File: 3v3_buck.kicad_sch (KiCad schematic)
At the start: 7 parts, among them U1101 TLV62569DBVR

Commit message: added net tie to stepper motor PGND + various routing
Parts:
- NT1101: footprint BR_Virtual_Parts:NetTie-2_SMD_Pad_3.88mm_wide -> BR_Virtual_Parts:NetTie-2_SMD_Pad_0.18mm_wide; symbol BR_Virtual_Parts:NetTie-2_3.88mm -> BR_Virtual_Parts:NetTie-2_0.18mm
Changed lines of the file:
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@@
 	)
 	(symbol
-		(lib_id "BR_Virtual_Parts:NetTie-2_3.88mm")
+		(lib_id "BR_Virtual_Parts:NetTie-2_0.18mm")
 		(at 130.81 106.68 90)
 		(unit 1)
-		(exclude_from_sim yes)
+		(exclude_from_sim no)
 		(in_bom no)
 		(on_board yes)
@@
 			)
 		)
-		(property "Footprint" "BR_Virtual_Parts:NetTie-2_SMD_Pad_3.88mm_wide"
-			(at 130.81 106.68 0)
+		(property "Footprint" "BR_Virtual_Parts:NetTie-2_SMD_Pad_0.18mm_wide"
+			(at 131.064 105.664 90)
 			(effects
 				(font
@@
 		)
 		(property "Datasheet" "~"
-			(at 130.81 106.68 0)
+			(at 125.73 97.79 0)
 			(effects
 				(font
@@
 		)
 		(property "Manufacturer" "~"
-			(at 130.81 106.68 0)
+			(at 111.76 104.14 0)
 			(effects
 				(font
 					(size 1.27 1.27)
 				)
+				(justify left)
 				(hide yes)
 			)
 		)
 		(property "Supplier 1" "~"
-			(at 130.81 106.68 0)
+			(at 109.22 104.14 0)
 			(effects
 				(font
 					(size 1.27 1.27)
 				)
+				(justify left)
 				(hide yes)
 			)
 		)
 		(property "Supplier Part Num 1" "~"
-			(at 130.81 106.68 0)
+			(at 106.68 104.14 0)
 			(effects
 				(font
 					(size 1.27 1.27)
 				)
+				(justify left)
 				(hide yes)
 			)
 		)
 		(property "Supplier 2" "~"
-			(at 130.81 106.68 0)
+			(at 104.14 104.14 0)
 			(effects
 				(font
 					(size 1.27 1.27)
 				)
+				(justify left)
 				(hide yes)
 			)
 		)
 		(property "Supplier Part Num 2" "~"
-			(at 130.81 106.68 0)
+			(at 101.6 104.14 0)
 			(effects
 				(font
 					(size 1.27 1.27)
 				)
+				(justify left)
 				(hide yes)
 			)
 		)
 		(property "Supplier 3" "~"
-			(at 130.81 106.68 0)
+			(at 99.06 104.14 0)
 			(effects
 				(font
 					(size 1.27 1.27)
 				)
+				(justify left)
 				(hide yes)
 			)
 		)
 		(property "Supplier Part Num 3" "~"
-			(at 130.81 106.68 0)
+			(at 96.52 104.14 0)
 			(effects
 				(font
 					(size 1.27 1.27)
 				)
+				(justify left)
 				(hide yes)
 			)
 		)
 		(property "Manufacturer Part Num" "~"
-			(at 130.81 106.68 0)
+			(at 93.98 104.14 0)
 			(effects
 				(font
 					(size 1.27 1.27)
 				)
+				(justify left)
 				(hide yes)
 			)

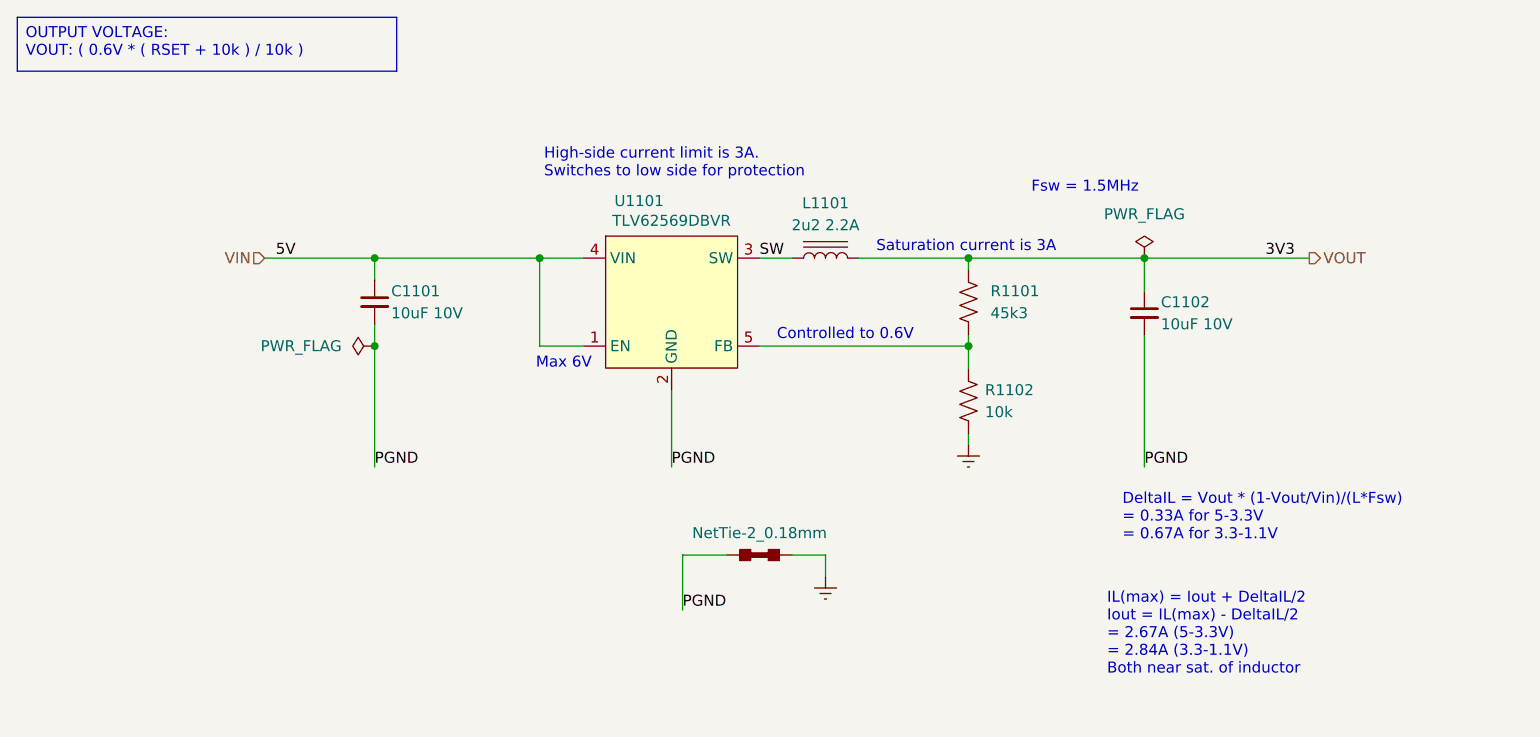
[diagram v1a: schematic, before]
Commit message: adding test pads + minor schematic edits
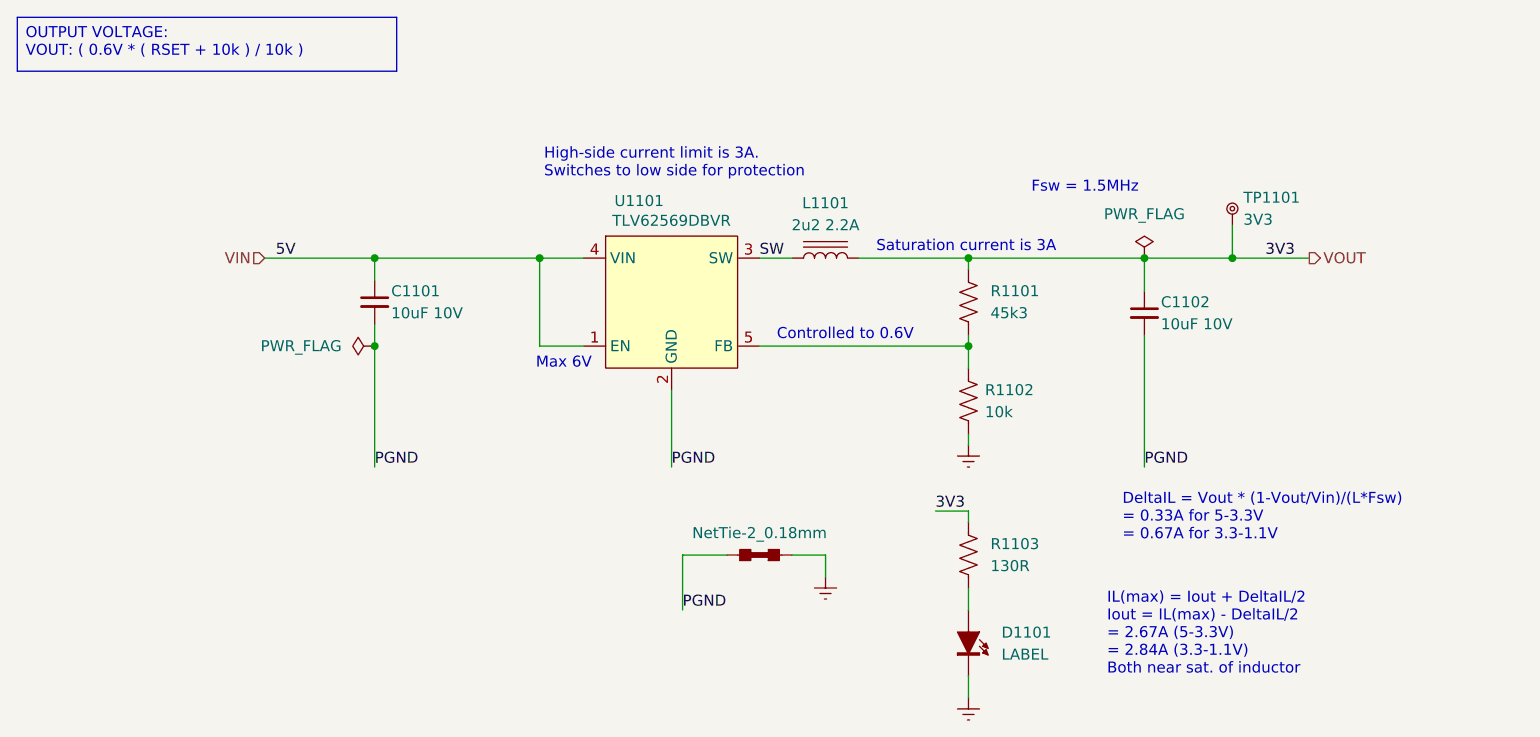
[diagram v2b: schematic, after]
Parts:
- added D1101: LABEL, BR_Optoelectronics:LED_0603_1608Metric, symbol BR_Optoelectronic:LTST-C191KGKT
- added R1103: 130R, BR_Passives:C_0402_1005Metric-minimized, symbol BR_Resistors_0402:R_0402_130R
- added TP1101: 3V3, BR_Connectors:TEST-TH_BD2.54-P1.4_RED, symbol BR_Connectors:TP_Ring_PTH
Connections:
- net GND: now also D1101.1 (K)
- net VOUT: now also R1103.1, TP1101.1
- new net: D1101.2 (A), R1103.2

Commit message: preboard review of updates
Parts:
- R1103: value 130R -> 1k3; symbol BR_Resistors_0402:R_0402_130R -> BR_Resistors_0402:R_0402_1k3; BRE Number BRE-000301 -> BRE-001251; JLCPCB Part Num C477610 -> C185455; Manufacturer Part Num RC0402FR-07130RL -> RC0402FR-071K3L; Supplier 2 Mouser -> DigiKey; Supplier Part Num 1 311-130LRCT-ND -> YAG3036CT-ND; Supplier Part Num 2 603-RC0402FR-07130RL -> YAG3036CT-ND; Supplier Part Num 3 C477610 -> C185455
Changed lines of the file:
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@@
 	)
 	(symbol
-		(lib_id "BR_Resistors_0402:R_0402_130R")
+		(lib_id "BR_Resistors_0402:R_0402_1k3")
 		(at 154.94 106.68 0)
 		(unit 1)
@@
 			)
 		)
-		(property "Value" "130R"
+		(property "Value" "1k3"
 			(at 157.48 107.9499 0)
 			(effects
@@
 			)
 		)
-		(property "Description" "130R 1% 100ppm 62.5mW Thick Film Resistor 0402"
+		(property "Description" "1.3k 1% 100ppm 62.5mW Thick Film Resistor 0402"
 			(at 154.94 43.18 0)
 			(effects
@@
 			)
 		)
-		(property "Manufacturer Part Num" "RC0402FR-07130RL"
+		(property "Manufacturer Part Num" "RC0402FR-071K3L"
 			(at 154.94 38.1 0)
 			(effects
@@
 			)
 		)
-		(property "BRE Number" "BRE-000301"
+		(property "BRE Number" "BRE-001251"
 			(at 154.94 40.64 0)
 			(effects
@@
 			)
 		)
-		(property "Supplier Part Num 1" "311-130LRCT-ND"
+		(property "Supplier Part Num 1" "YAG3036CT-ND"
 			(at 154.94 48.26 0)
 			(effects
@@
 			)
 		)
-		(property "Supplier 2" "Mouser"
+		(property "Supplier 2" "DigiKey"
 			(at 154.94 50.8 0)
 			(effects
@@
 			)
 		)
-		(property "Supplier Part Num 2" "603-RC0402FR-07130RL"
+		(property "Supplier Part Num 2" "YAG3036CT-ND"
 			(at 154.94 53.34 0)
 			(effects
@@
 			)
 		)
-		(property "Supplier Part Num 3" "C477610"
+		(property "Supplier Part Num 3" "C185455"
 			(at 154.94 58.42 0)
 			(effects
@@
 			)
 		)
-		(property "JLCPCB Part Num" "C477610"
+		(property "JLCPCB Part Num" "C185455"
 			(at 154.94 60.96 0)
 			(effects

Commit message: various improvements
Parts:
- D1101: value LABEL -> 3V3
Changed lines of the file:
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@@
 			)
 		)
-		(property "Value" "LABEL"
+		(property "Value" "3V3"
 			(at 158.75 118.1734 90)
 			(effects

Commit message: last checks + board characteristics tables
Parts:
- added TP1102: GND, BR_Connectors:TEST-TH_BD2.54-P1.4_RED, symbol BR_Connectors:TP_Ring_PTH
- C1101, C1102: JLCPCB Part Num (none) -> C315248
- L1101: JLCPCB Part Num (none) -> C2041550
- R1102: JLCPCB Part Num (none) -> C106225
- U1101: JLCPCB Part Num (none) -> C141836
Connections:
- net GND: now also TP1102.1

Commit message: refactoring tx a bit
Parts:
- NT1101: value NetTie-2_0.18mm -> Net_Tie_0201; footprint BR_Virtual_Parts:NetTie-2_SMD_Pad_0.18mm_wide -> BR_Virtual_Parts:Net_Tie_0201_1608Metric; symbol BR_Virtual_Parts:NetTie-2_0.18mm -> BR_Virtual_Parts:Net_Tie_0201
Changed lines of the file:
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@@
 	)
 	(symbol
-		(lib_id "BR_Virtual_Parts:NetTie-2_0.18mm")
+		(lib_id "BR_Virtual_Parts:Net_Tie_0201")
 		(at 130.81 106.68 90)
 		(unit 1)
@@
 			)
 		)
-		(property "Value" "NetTie-2_0.18mm"
+		(property "Value" "Net_Tie_0201"
 			(at 130.81 104.14 90)
 			(effects
@@
 			)
 		)
-		(property "Footprint" "BR_Virtual_Parts:NetTie-2_SMD_Pad_0.18mm_wide"
+		(property "Footprint" "BR_Virtual_Parts:Net_Tie_0201_1608Metric"
 			(at 131.064 105.664 90)
 			(effects
